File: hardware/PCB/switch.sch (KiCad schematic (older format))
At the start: 136 parts

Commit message: making progress
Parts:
- D1, D10, D11, D12, D13, D14, D15, D16, D17, D18, D19, D2, D20, D21, D22, D23, D24, D25, D26, D27, D28, D29, D3, D30, D31, D32, D33, D34, D35, D36, D37, D38, D39, D4, D40, D41, D42, D43, D44, D45, D46, D47, D48, D49, D5, D50, D51, D52, D53, D54, D55, D56, D57, D58, D59, D6, D60, D61, D62, D63, D64, D65, D66, D67, D68, D7, D8, D9: value 1N4148W -> 1N4148WS
- Key1, Key10, Key11, Key12, Key13, Key14, Key15, Key16, Key17, Key18, Key19, Key2, Key20, Key21, Key22, Key23, Key24, Key25, Key26, Key27, Key28, Key29, Key3, Key30, Key31, Key32, Key33, Key34, Key35, Key36, Key37, Key38, Key39, Key4, Key40, Key41, Key42, Key43, Key44, Key45, Key46, Key47, Key48, Key49, Key5, Key50, Key51, Key52, Key53, Key54, Key55, Key56, Key57, Key58, Key59, Key6, Key60, Key61, Key62, Key63, Key64, Key65, Key66, Key67, Key68, Key7, Key8, Key9: value SW_SPST -> CPG151101S03

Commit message: Now it should be working just fine
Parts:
- D1, D10, D11, D12, D13, D14, D15, D16, D17, D18, D19, D2, D20, D21, D22, D23, D24, D25, D26, D27, D28, D29, D3, D30, D31, D32, D33, D34, D35, D36, D37, D38, D39, D4, D40, D41, D42, D43, D44, D45, D46, D47, D48, D49, D5, D50, D51, D52, D53, D54, D55, D56, D57, D58, D59, D6, D60, D61, D62, D63, D64, D65, D66, D67, D68, D7, D8, D9: Footprint Diode_SMD:D_SOD-323 -> (none); Value 1N4148W -> (none)
- Key1, Key10, Key11, Key12, Key13, Key14, Key15, Key16, Key17, Key18, Key19, Key2, Key20, Key21, Key22, Key23, Key24, Key25, Key26, Key27, Key28, Key29, Key3, Key30, Key31, Key32, Key33, Key34, Key35, Key36, Key37, Key38, Key39, Key4, Key40, Key41, Key42, Key43, Key44, Key45, Key46, Key47, Key48, Key49, Key5, Key50, Key51, Key52, Key53, Key54, Key55, Key56, Key57, Key58, Key59, Key6, Key60, Key61, Key62, Key63, Key64, Key65, Key66, Key67, Key68, Key7, Key8, Key9: Footprint keyswitches:Kailh_socket_MX_optional_reversible -> (none)

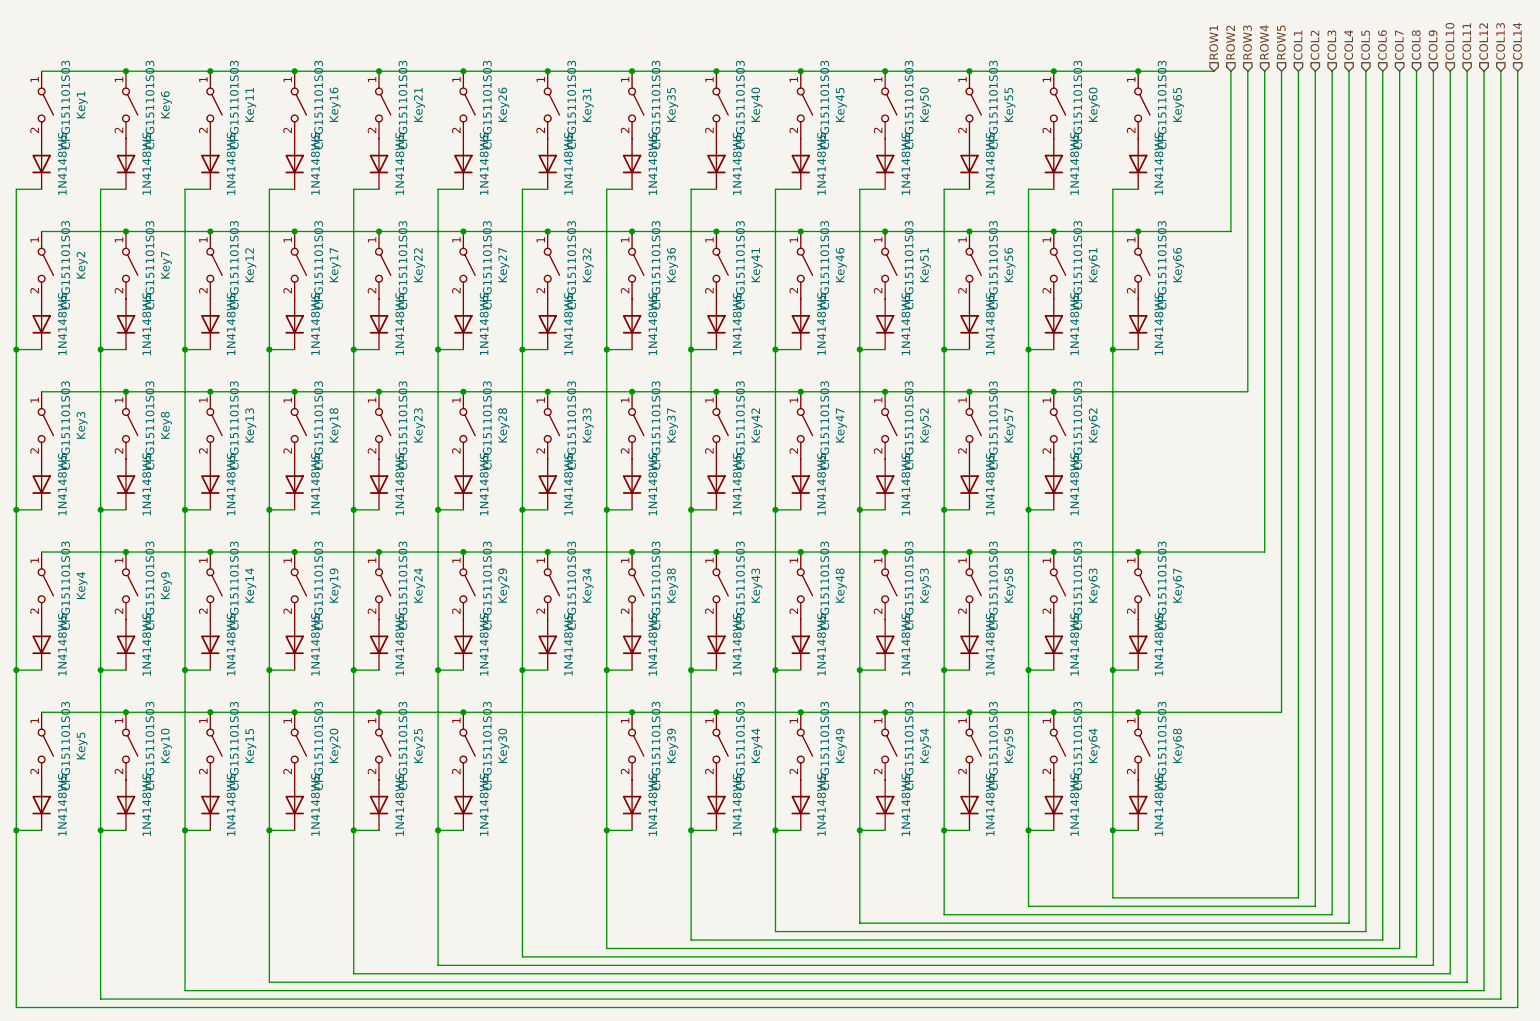
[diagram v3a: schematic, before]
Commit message: add in part number so I could use it for the bom
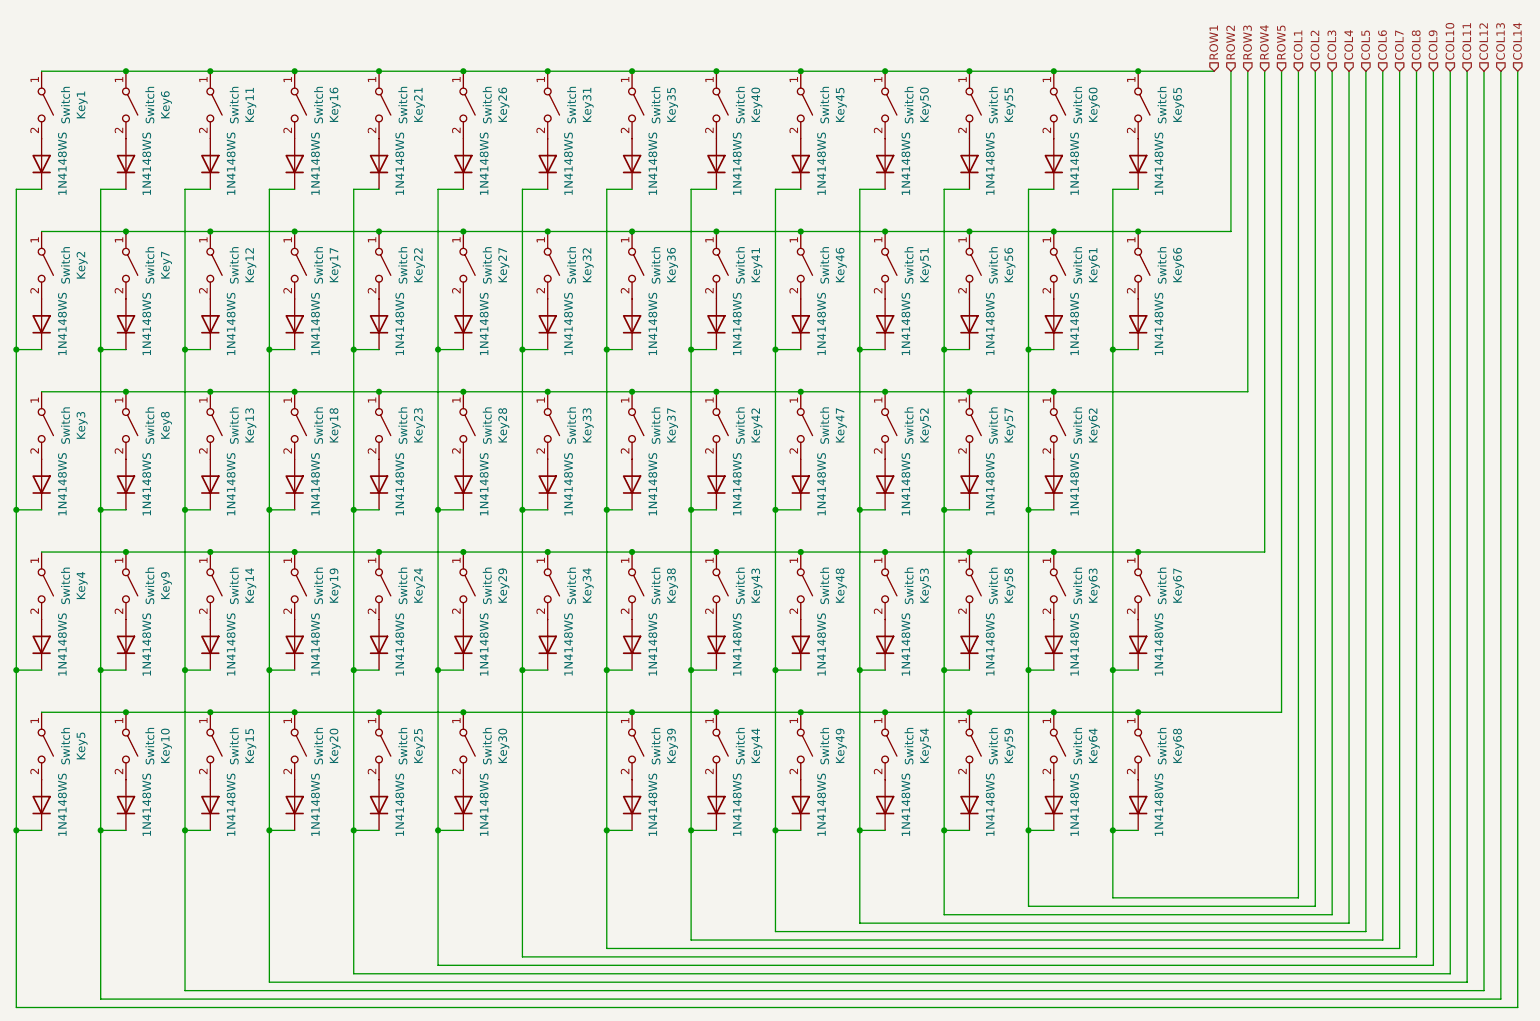
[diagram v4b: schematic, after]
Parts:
- D1, D10, D11, D12, D13, D14, D15, D16, D17, D18, D19, D2, D20, D21, D22, D23, D24, D25, D26, D27, D28, D29, D3, D30, D31, D32, D33, D34, D35, D36, D37, D38, D39, D4, D40, D41, D42, D43, D44, D45, D46, D47, D48, D49, D5, D50, D51, D52, D53, D54, D55, D56, D57, D58, D59, D6, D60, D61, D62, D63, D64, D65, D66, D67, D68, D7, D8, D9: Part Number (none) -> 1N4148WS
- Key1, Key10, Key11, Key12, Key13, Key14, Key15, Key16, Key17, Key18, Key19, Key2, Key20, Key21, Key22, Key23, Key24, Key25, Key26, Key27, Key28, Key29, Key3, Key30, Key31, Key32, Key33, Key34, Key35, Key36, Key37, Key38, Key39, Key4, Key40, Key41, Key42, Key43, Key44, Key45, Key46, Key47, Key48, Key49, Key5, Key50, Key51, Key52, Key53, Key54, Key55, Key56, Key57, Key58, Key59, Key6, Key60, Key61, Key62, Key63, Key64, Key65, Key66, Key67, Key68, Key7, Key8, Key9: value CPG151101S03 -> Switch; Part Number (none) -> CPG151101S11

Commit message: Rev 0.5
1. Use a better 1205 LED (much chaper on LCSC)
2. Fix the crystal CL, Rext
3. did a better job on wiring (but might come with power issues?)
4. fix the key position (0.01mm shifted so its a big fix)
5. generate better bom files
6. add in LCSC and part number so easier to source
0.4 is gone
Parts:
- D1, D10, D11, D12, D13, D14, D15, D16, D17, D18, D19, D2, D20, D21, D22, D23, D24, D25, D26, D27, D28, D29, D3, D30, D31, D32, D33, D34, D35, D36, D37, D38, D39, D4, D40, D41, D42, D43, D44, D45, D46, D47, D48, D49, D5, D50, D51, D52, D53, D54, D55, D56, D57, D58, D59, D6, D60, D61, D62, D63, D64, D65, D66, D67, D68, D7, D8, D9: LCSC (none) -> C118873
